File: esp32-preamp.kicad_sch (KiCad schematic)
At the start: 4 parts, among them U1 ESP32 D1 Mini, U2 PGA2311

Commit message: progress!
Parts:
- removed U2: PGA2311, PGA2311U_1K:SOIC127P1030X265-16N, symbol PGA2311:PGA2311U_1K
- added C1, C2: 10uF, symbol Device:C
- added C3: 10uF, symbol Device:C_Polarized
- added D1, D2, D3, D4: 1N4004, Diode_THT:D_DO-41_SOD81_P10.16mm_Horizontal, symbol Diode:1N4004
- added J2: OUT, symbol Connector:Conn_01x03_Pin
- added J3: LFE, symbol Connector:Conn_01x02_Pin
- added J4: INPUT 1, symbol Connector:Conn_01x03_Pin
- added J5, J6: INPUT 2, symbol Connector:Conn_01x03_Pin
- added J7: TSOP382, symbol Connector:Conn_01x03_Pin
- added J7: AMP SLEEP, symbol Connector:Conn_01x02_Pin
- added J8: DIAL, symbol Connector:Conn_01x03_Pin
- added K1, K2, K3, K4: (no value), symbol Relay:TQ2
- added Q2, Q3, Q4, Q5: 2N3904, Package_TO_SOT_THT:TO-92_Inline, symbol Transistor_BJT:2N3904
- added U1: TSR0.5-2450, Converter_DCDC:Converter_DCDC_TRACO_TSR0.5-24xx_TSR0.5-24xxx_THT, symbol Converter_DCDC:TSR0.5-2450
- added U2: (no value), symbol Device:PGA2311
- added U2: (no value), symbol Power_Management:LM2660
- renumbered U1 to U3
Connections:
- net +5V: now also U1.3 (Vout), U2.12 (+5V_A), U2.4 (+5V_D), U2.8 (V+)
- net at R1.1: now also J2.3 (Pin_3), U2.14 (OUT_L)
- net at R1.2: now also R2.2, J3.2 (Pin_2)
- net at R2.1: now also J2.2 (Pin_2), U2.11 (OUT_R)
- net +3.3V: now reaches U3.16 (3V3)
- net +3.3V: now also J7.3 (Pin_3)
- net GNDD renamed GNDA
- net GNDA: now also C2.2, J2.1 (Pin_1), J3.1 (Pin_1), J4.3 (Pin_3), J5.3 (Pin_3), J6.3 (Pin_3), U1.2 (GND), U2.10 (AGND_R), U2.15 (AGND_L), U2.3 (GND), U2.5 (GND_D), U2.6 (LV)
- new net: C1.1, U2.2 (CAP+)
- new net: C1.2, U2.4 (CAP-)
- new net: D1.2 (A), K1.10 (GND), Q2.3 (C)
- new net: J4.1 (Pin_1), K1.4 (NO1)
- new net: J4.2 (Pin_2), K1.7 (NO2)
- new net: D3.2 (A), K3.10 (GND), Q4.3 (C)
- new net: J6.1 (Pin_1), K3.4 (NO1)
- new net: J6.2 (Pin_2), K3.7 (NO2)
- new net: D2.2 (A), K2.10 (GND), Q3.3 (C)
- new net: D4.2 (A), K4.10 (GND), Q5.3 (C)
- new net: J5.1 (Pin_1), K2.4 (NO1)
- new net: J5.2 (Pin_2), K2.7 (NO2)
- new net: J7.1 (Pin_1), K4.4 (NO1)
- new net: J7.2 (Pin_2), K4.3 (COM1)
- new net +12V: C3.1, D1.1 (K), D2.1 (K), D3.1 (K), D4.1 (K), K1.1 (12V), K2.1 (12V), K3.1 (12V), K4.1 (12V), U1.1 (Vin)
- new net -5V: C2.1, U2.13 (-5V_A), U2.5 (OUT)
- new net CS: U2.2 (CS)
- new net GNDS: C3.2, J7.2 (Pin_2), Q2.1 (E), Q3.1 (E), Q4.1 (E), Q5.1 (E)
- new net IN_L: K1.3 (COM1), K2.3 (COM1), K3.3 (COM1), U2.16 (IN_L)
- new net IN_R: K1.8 (COM2), K2.8 (COM2), K3.8 (COM2), U2.9 (IN_R)
- new net MUTE: U2.8 (MUTE)
- new net SCLK: U2.6 (SCLK)
- new net SDI: U2.3 (SDI)
- new net SDO: U2.7 (SDO)
- new net TSOP382: J7.1 (Pin_1)
- new net ZCEN: U2.1 (ZCEN)
- no-connect marks 1 -> 4
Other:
- note added: "POWER"
- moved on the sheet: R1

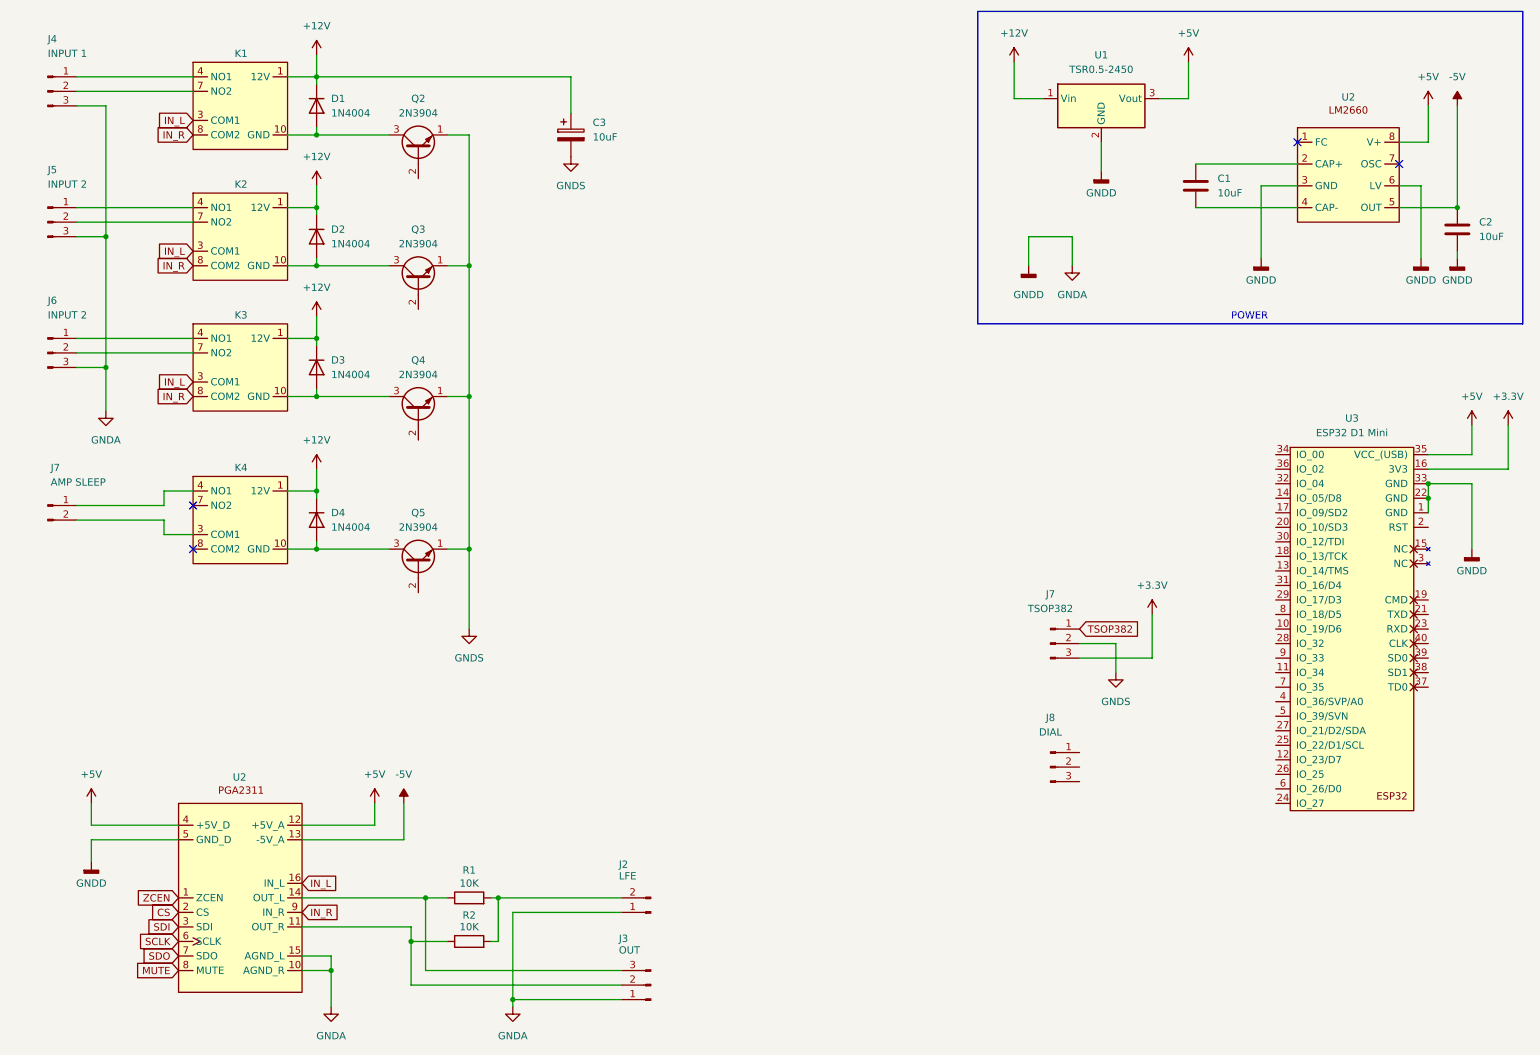
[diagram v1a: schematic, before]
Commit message: Add motor circuit
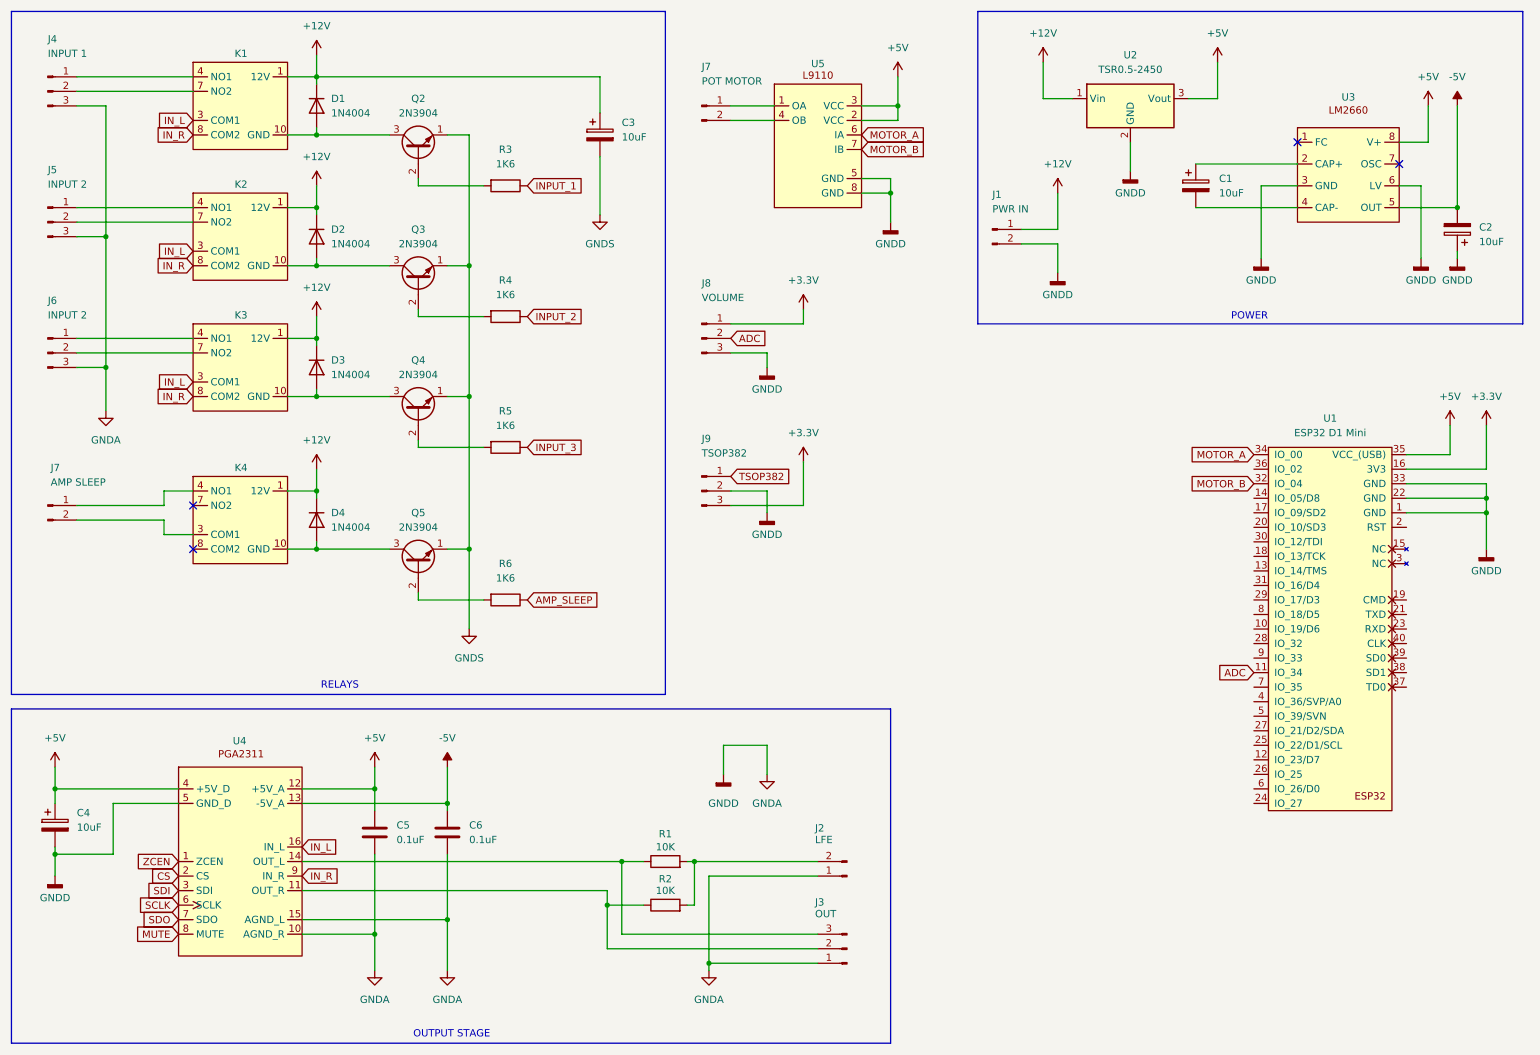
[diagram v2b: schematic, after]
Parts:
- added C4: 10uF, symbol Device:C_Polarized
- added C5, C6: 0.1uF, symbol Device:C
- added J1: PWR IN, symbol Connector:Conn_01x02_Pin
- added J7: POT MOTOR, symbol Connector:Conn_01x02_Pin
- added R3, R4, R5, R6: 1K6, symbol Device:R
- added U5: (no value), symbol Motor:L9110
- C1, C2: symbol Device:C -> Device:C_Polarized
- J8: value DIAL -> VOLUME
- renumbered J7 to J9, U3 to U1, U1 to U2, U2 to U3, U2 to U4
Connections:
- net +12V: now also J1.1 (Pin_1)
- net +3.3V: now also J8.1 (Pin_1)
- net +5V: now also C4.1, C5.1, U5.2 (VCC), U5.3 (VCC)
- net -5V: now also C2.2, C6.1; no longer C2.1
- net GNDA: now also C2.1, J8.3 (Pin_3), J9.2 (Pin_2), C4.2, C5.2, C6.2, J1.2 (Pin_2), U5.5 (GND), U5.8 (GND); no longer C2.2
- net GNDS: no longer J9.2 (Pin_2)
- net at Q3.2 (B): now also R4.2
- net at Q5.2 (B): now also R6.2
- net at Q4.2 (B): now also R5.2
- net at Q2.2 (B): now also R3.2
- net ADC: now reaches U1.11 (IO_34)
- net ADC: now also J8.2 (Pin_2)
- net MOTOR_B: now reaches U1.32 (IO_04)
- net MOTOR_B: now also U5.7 (IB)
- net MOTOR_A: now reaches U1.34 (IO_00)
- net MOTOR_A: now also U5.6 (IA)
- new net: J7.1 (Pin_1), U5.1 (OA)
- new net: J7.2 (Pin_2), U5.4 (OB)
- new net AMP_SLEEP: R6.1
- new net INPUT_1: R3.1
- new net INPUT_2: R4.1
- new net INPUT_3: R5.1
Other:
- note added: "OUTPUT STAGE"
- note added: "RELAYS"
- moved on the sheet: C3, J2, J3, J8, J9, R1, R2, U1, U2, U4

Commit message: Repair duplicates
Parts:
- J7: value AMP SLEEP -> AMP PWR
- renumbered J9 to J10, J7 to J8, J8 to J9, Q2 to Q1, Q3 to Q2, Q4 to Q3, Q5 to Q4, R3 to R1, R4 to R2, R5 to R3, R6 to R4, R1 to R5, R2 to R6
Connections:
- net AMP_SLEEP renamed AMP_PWR
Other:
- title: (none) -> ESP32 Volume Control
- moved on the sheet: U1

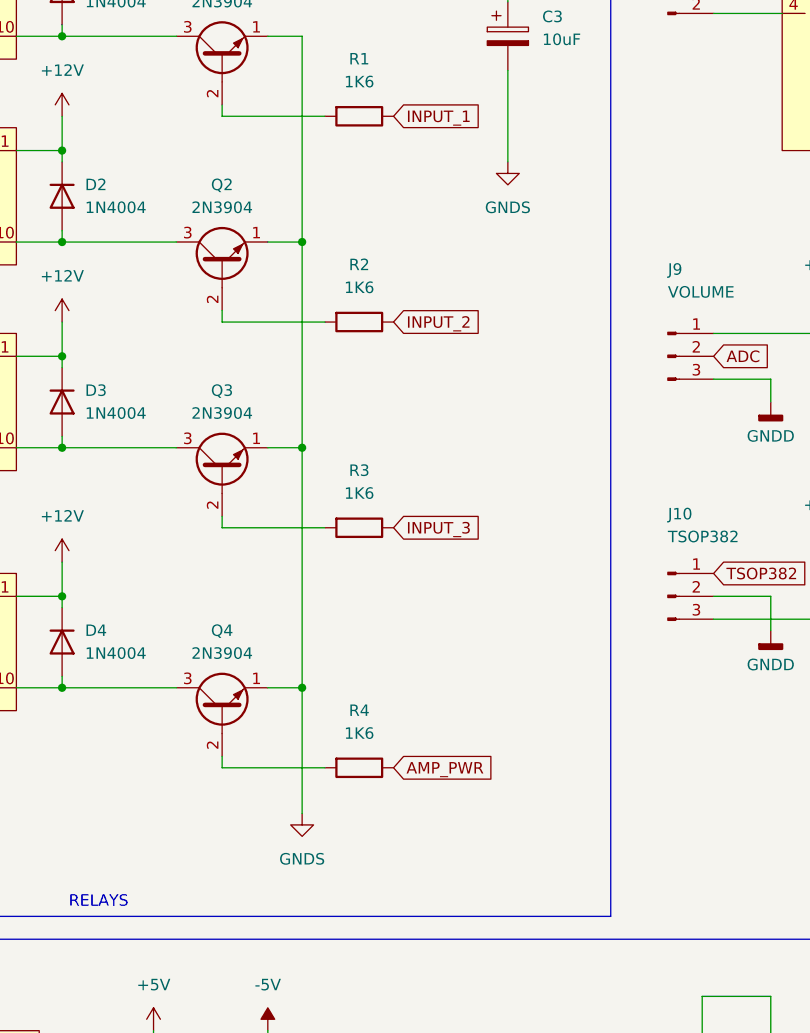
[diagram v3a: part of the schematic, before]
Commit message: Remove GNDS references
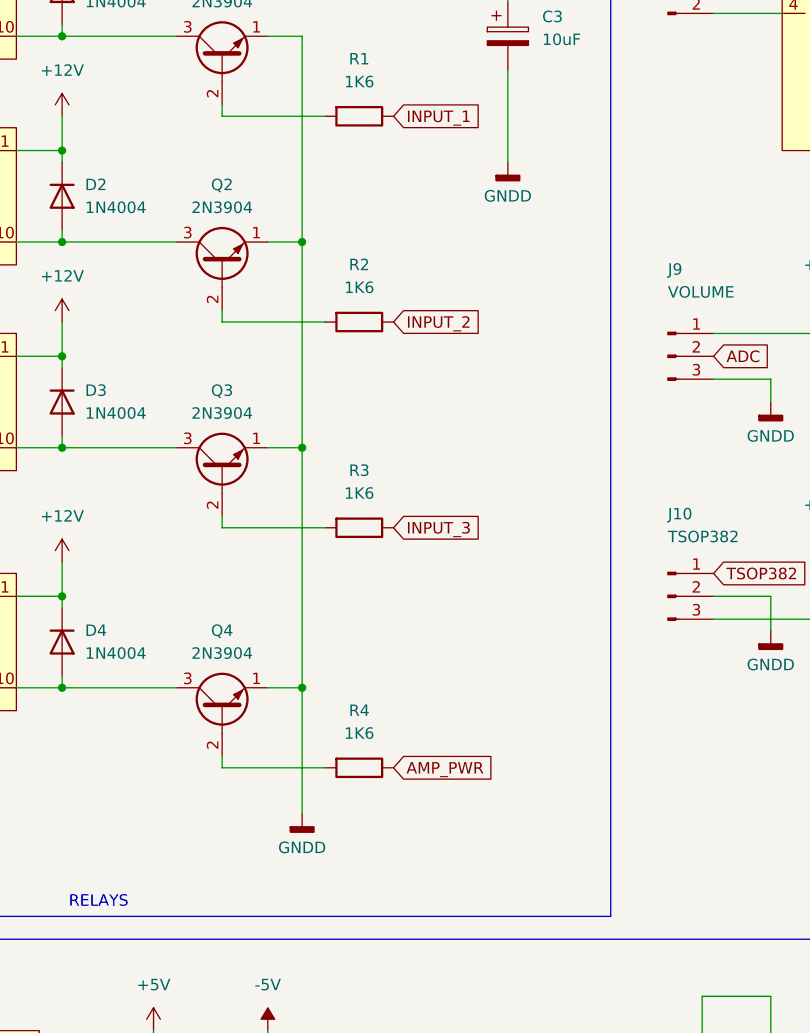
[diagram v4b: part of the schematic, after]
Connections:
- net GNDS is gone; now on net GNDA: C3.2, Q1.1 (E), Q2.1 (E), Q3.1 (E), Q4.1 (E)
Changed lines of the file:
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@@
 	(symbol
 		(lib_id "power:GNDD")
+		(at 121.92 50.8 0)
+		(unit 1)
+		(body_style 1)
+		(exclude_from_sim no)
+		(in_bom yes)
+		(on_board yes)
+		(in_pos_files yes)
+		(dnp no)
+		(fields_autoplaced yes)
+		(property "Reference" "#PWR027"
+			(at 121.92 57.15 0)
+			(hide yes)
+			(show_name no)
+			(do_not_autoplace no)
+			(effects
+				(font
+					(size 1.27 1.27)
+				)
+			)
+		)
+		(property "Value" "GNDD"
+			(at 121.92 54.61 0)
+			(show_name no)
+			(do_not_autoplace no)
+			(effects
+				(font
+					(size 1.27 1.27)
+				)
+			)
+		)
+		(property "Footprint" ""
+			(at 121.92 50.8 0)
+			(hide yes)
+			(show_name no)
+			(do_not_autoplace no)
+			(effects
+				(font
+					(size 1.27 1.27)
+				)
+			)
+		)
+		(property "Datasheet" ""
+			(at 121.92 50.8 0)
+			(hide yes)
+			(show_name no)
+			(do_not_autoplace no)
+			(effects
+				(font
+					(size 1.27 1.27)
+				)
+			)
+		)
+		(property "Description" "Power symbol creates a global label with name \"GNDD\" , digital ground"
+			(at 121.92 50.8 0)
+			(hide yes)
+			(show_name no)
+			(do_not_autoplace no)
+			(effects
+				(font
+					(size 1.27 1.27)
+				)
+			)
+		)
+		(pin "1"
+		)
+		(instances
+			(project "esp32-preamp"
+				(path "/ef07d777-d2fe-4af3-a209-ac0ed59e2bee"
+					(reference "#PWR027")
+					(unit 1)
+				)
+			)
+		)
+	)
+	(symbol
+		(lib_id "power:GNDD")
 		(at 172.72 52.07 0)
 		(unit 1)
@@
 	)
 	(symbol
-		(lib_id "power:GNDS")
-		(at 99.06 123.19 0)
-		(unit 1)
-		(body_style 1)
-		(exclude_from_sim no)
-		(in_bom yes)
-		(on_board yes)
-		(in_pos_files yes)
-		(dnp no)
-		(fields_autoplaced yes)
-		(property "Reference" "#PWR027"
-			(at 99.06 129.54 0)
-			(hide yes)
-			(show_name no)
-			(do_not_autoplace no)
-			(effects
-				(font
-					(size 1.27 1.27)
-				)
-			)
-		)
-		(property "Value" "GNDS"
-			(at 99.06 128.27 0)
-			(show_name no)
-			(do_not_autoplace no)
-			(effects
-				(font
-					(size 1.27 1.27)
-				)
-			)
-		)
-		(property "Footprint" ""
-			(at 99.06 123.19 0)
-			(hide yes)
-			(show_name no)
-			(do_not_autoplace no)
-			(effects
-				(font
-					(size 1.27 1.27)
-				)
-			)
-		)
-		(property "Datasheet" ""
-			(at 99.06 123.19 0)
-			(hide yes)
-			(show_name no)
-			(do_not_autoplace no)
-			(effects
-				(font
-					(size 1.27 1.27)
-				)
-			)
-		)
-		(property "Description" "Power symbol creates a global label with name \"GNDS\" , signal ground"
-			(at 99.06 123.19 0)
-			(hide yes)
-			(show_name no)
-			(do_not_autoplace no)
-			(effects
-				(font
-					(size 1.27 1.27)
-				)
-			)
-		)
-		(pin "1"
-		)
-		(instances
-			(project "esp32-preamp"
-				(path "/ef07d777-d2fe-4af3-a209-ac0ed59e2bee"
-					(reference "#PWR027")
-					(unit 1)
-				)
-			)
-		)
-	)
-	(symbol
 		(lib_id "power:-5V")
 		(at 271.78 31.75 0)
@@
 	)
 	(symbol
+		(lib_id "power:GNDD")
+		(at 99.06 123.19 0)
+		(unit 1)
+		(body_style 1)
+		(exclude_from_sim no)
+		(in_bom yes)
+		(on_board yes)
+		(in_pos_files yes)
+		(dnp no)
+		(fields_autoplaced yes)
+		(property "Reference" "#PWR024"
+			(at 99.06 129.54 0)
+			(hide yes)
+			(show_name no)
+			(do_not_autoplace no)
+			(effects
+				(font
+					(size 1.27 1.27)
+				)
+			)
+		)
+		(property "Value" "GNDD"
+			(at 99.06 127 0)
+			(show_name no)
+			(do_not_autoplace no)
+			(effects
+				(font
+					(size 1.27 1.27)
+				)
+			)
+		)
+		(property "Footprint" ""
+			(at 99.06 123.19 0)
+			(hide yes)
+			(show_name no)
+			(do_not_autoplace no)
+			(effects
+				(font
+					(size 1.27 1.27)
+				)
+			)
+		)
+		(property "Datasheet" ""
+			(at 99.06 123.19 0)
+			(hide yes)
+			(show_name no)
+			(do_not_autoplace no)
+			(effects
+				(font
+					(size 1.27 1.27)
+				)
+			)
+		)
+		(property "Description" "Power symbol creates a global label with name \"GNDD\" , digital ground"
+			(at 99.06 123.19 0)
+			(hide yes)
+			(show_name no)
+			(do_not_autoplace no)
+			(effects
+				(font
+					(size 1.27 1.27)
+				)
+			)
+		)
+		(pin "1"
+		)
+		(instances
+			(project "esp32-preamp"
+				(path "/ef07d777-d2fe-4af3-a209-ac0ed59e2bee"
+					(reference "#PWR024")
+					(unit 1)
+				)
+			)
+		)
+	)
+	(symbol
 		(lib_id "Transistor_BJT:2N3904")
 		(at 90.17 85.09 90)
@@
 					(unit 1)
 				)
-			)
-		)
-	)
-	(symbol
-		(lib_id "power:GNDS")
-		(at 121.92 50.8 0)
-		(unit 1)
-		(body_style 1)
-		(exclude_from_sim no)
-		(in_bom yes)
-		(on_board yes)
-		(in_pos_files yes)
-		(dnp no)
-		(fields_autoplaced yes)
-		(property "Reference" "#PWR024"
-			(at 121.92 57.15 0)
-			(hide yes)
-			(show_name no)
-			(do_not_autoplace no)
-			(effects
-				(font
-					(size 1.27 1.27)
-				)
-			)
-		)
-		(property "Value" "GNDS"
-			(at 121.92 55.88 0)
-			(show_name no)
-			(do_not_autoplace no)
-			(effects
-				(font
-					(size 1.27 1.27)
-				)
-			)
-		)
-		(property "Footprint" ""
-			(at 121.92 50.8 0)
-			(hide yes)
-			(show_name no)
-			(do_not_autoplace no)
-			(effects
-				(font
-					(size 1.27 1.27)
-				)
-			)
-		)
-		(property "Datasheet" ""
-			(at 121.92 50.8 0)
-			(hide yes)
-			(show_name no)
-			(do_not_autoplace no)
-			(effects
-				(font
-					(size 1.27 1.27)
-				)
-			)
-		)
-		(property "Description" "Power symbol creates a global label with name \"GNDS\" , signal ground"
-			(at 121.92 50.8 0)
-			(hide yes)
-			(show_name no)
-			(do_not_autoplace no)
-			(effects
-				(font
-					(size 1.27 1.27)
-				)
-			)
-		)
-		(pin "1"
-		)
-		(instances
-			(project "esp32-preamp"
-				(path "/ef07d777-d2fe-4af3-a209-ac0ed59e2bee"
-					(reference "#PWR024")
-					(unit 1)
-				)

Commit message: Add jumper
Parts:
- added R7: 0R, symbol Device:R
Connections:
- net GNDA: now also R7.2; no longer C2.1, C3.2, C4.2, J1.2 (Pin_2), J10.2 (Pin_2), J9.3 (Pin_3), Q1.1 (E), Q2.1 (E), Q3.1 (E), Q4.1 (E), U1.1 (GND), U1.22 (GND), U1.33 (GND), U2.2 (GND), U3.3 (GND), U3.6 (LV), U4.5 (GND_D), U5.5 (GND), U5.8 (GND)
- new net GNDD: C2.1, C3.2, C4.2, J1.2 (Pin_2), J10.2 (Pin_2), J9.3 (Pin_3), Q1.1 (E), Q2.1 (E), Q3.1 (E), Q4.1 (E), R7.1, U1.1 (GND), U1.22 (GND), U1.33 (GND), U2.2 (GND), U3.3 (GND), U3.6 (LV), U4.5 (GND_D), U5.5 (GND), U5.8 (GND)
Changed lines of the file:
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@@
 	(wire
 		(pts
-			(xy 151.13 143.51) (xy 151.13 148.59)
+			(xy 151.13 144.78) (xy 151.13 148.59)
 		)
 		(stroke
@@
 	(wire
 		(pts
-			(xy 143.51 148.59) (xy 143.51 143.51)
+			(xy 143.51 148.59) (xy 143.51 144.78)
 		)
 		(stroke
@@
 	(wire
 		(pts
-			(xy 143.51 143.51) (xy 151.13 143.51)
-		)
-		(stroke
-			(width 0)
-			(type default)
-		)
-	)
-	(wire
-		(pts
 			(xy 95.25 36.83) (xy 99.06 36.83)
 		)
@@
 					(unit 1)
 				)
+			)
+		)
+	)
+	(symbol
+		(lib_id "Device:R")
+		(at 147.32 144.78 90)
+		(unit 1)
+		(body_style 1)
+		(exclude_from_sim no)
+		(in_bom yes)
+		(on_board yes)
+		(in_pos_files yes)
+		(dnp no)
+		(property "Reference" "R7"
+			(at 147.32 140.208 90)
+			(show_name no)
+			(do_not_autoplace no)
+			(effects
+				(font
+					(size 1.27 1.27)
+				)
+			)
+		)
+		(property "Value" "0R"
+			(at 147.32 141.986 90)
+			(show_name no)
+			(do_not_autoplace no)
+			(effects
+				(font
+					(size 1.27 1.27)
+				)
+			)
+		)
+		(property "Footprint" ""
+			(at 147.32 146.558 90)
+			(hide yes)
+			(show_name no)
+			(do_not_autoplace no)
+			(effects
+				(font
+					(size 1.27 1.27)
+				)
+			)
+		)
+		(property "Datasheet" ""
+			(at 147.32 144.78 0)
+			(hide yes)
+			(show_name no)
+			(do_not_autoplace no)
+			(effects
+				(font
+					(size 1.27 1.27)
+				)
+			)
+		)
+		(property "Description" "Resistor"
+			(at 147.32 144.78 0)
+			(hide yes)
+			(show_name no)
+			(do_not_autoplace no)
+			(effects
+				(font
+					(size 1.27 1.27)
+				)
+			)
+		)
+		(pin "1"
+		)
+		(pin "2"
+		)
+		(instances
+			(project "esp32-preamp"
+				(path "/ef07d777-d2fe-4af3-a209-ac0ed59e2bee"
+					(reference "R7")
+					(unit 1)
+				)

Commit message: Prepare SDK lines
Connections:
- net AMP_PWR: now also U1.29 (IO_17/D3)
- net INPUT_1: now also U1.6 (IO_26/D0)
- net INPUT_2: now also U1.25 (IO_22/D1/SCL)
- net INPUT_3: now also U1.27 (IO_21/D2/SDA)
- net TSOP382: now also U1.8 (IO_18/D5)
